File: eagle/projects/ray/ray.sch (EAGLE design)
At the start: 4 parts

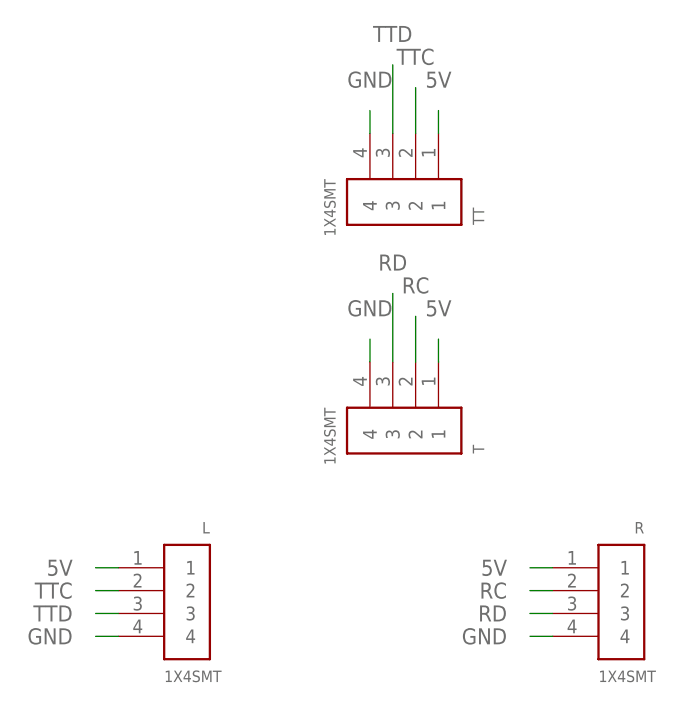
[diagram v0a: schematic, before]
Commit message: make solder pads for LED strips more forgiving
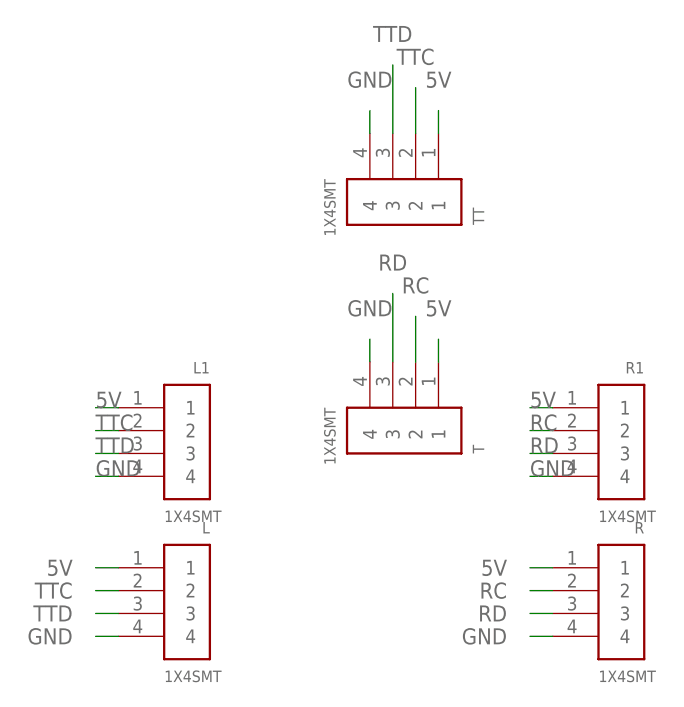
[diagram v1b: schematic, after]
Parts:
- added L1, R1: 1X4SMT, adafruit:1X4SMT
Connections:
- net 5V: now also L1.1, R1.1
- net GND: now also L1.4, R1.4
- net RC: now also R1.2
- net RD: now also R1.3
- net TTC: now also L1.2
- net TTD: now also L1.3
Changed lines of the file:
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@@
 <part name="R" library="adafruit" library_urn="urn:adsk.eagle:library:420" deviceset="1X4" device="SMT" package3d_urn="urn:adsk.eagle:package:6240933/1"/>
 <part name="TT" library="adafruit" library_urn="urn:adsk.eagle:library:420" deviceset="1X4" device="SMT" package3d_urn="urn:adsk.eagle:package:6240933/1"/>
+<part name="L1" library="adafruit" library_urn="urn:adsk.eagle:library:420" deviceset="1X4" device="SMT" package3d_urn="urn:adsk.eagle:package:6240933/1"/>
+<part name="R1" library="adafruit" library_urn="urn:adsk.eagle:library:420" deviceset="1X4" device="SMT" package3d_urn="urn:adsk.eagle:package:6240933/1"/>
 </parts>
 <sheets>
@@
 <attribute name="NAME" x="63.5" y="99.06" size="1.27" layer="95" font="vector" rot="R90"/>
 <attribute name="VALUE" x="45.72" y="104.14" size="1.27" layer="96" font="vector" rot="R270"/>
+</instance>
+<instance part="L1" gate="G$1" x="27.94" y="76.2" smashed="yes">
+<attribute name="NAME" x="33.02" y="83.82" size="1.27" layer="95" font="vector" rot="R180"/>
+<attribute name="VALUE" x="27.94" y="66.04" size="1.27" layer="96" font="vector"/>
+</instance>
+<instance part="R1" gate="G$1" x="76.2" y="76.2" smashed="yes">
+<attribute name="NAME" x="81.28" y="83.82" size="1.27" layer="95" font="vector" rot="R180"/>
+<attribute name="VALUE" x="76.2" y="66.04" size="1.27" layer="96" font="vector"/>
 </instance>
 </instances>
@@
 <label x="17.78" y="60.96" size="1.778" layer="95" align="center-right"/>
 </segment>
+<segment>
+<pinref part="L1" gate="G$1" pin="1"/>
+<wire x1="22.86" y1="78.74" x2="20.32" y2="78.74" width="0.1524" layer="91"/>
+<label x="20.32" y="78.74" size="1.778" layer="95"/>
+</segment>
+<segment>
+<pinref part="R1" gate="G$1" pin="1"/>
+<wire x1="71.12" y1="78.74" x2="68.58" y2="78.74" width="0.1524" layer="91"/>
+<label x="68.58" y="78.74" size="1.778" layer="95"/>
+</segment>
 </net>
 <net name="GND" class="0">
@@
 <label x="50.8" y="114.3" size="1.778" layer="95" align="bottom-center"/>
 </segment>
+<segment>
+<pinref part="L1" gate="G$1" pin="4"/>
+<wire x1="22.86" y1="71.12" x2="20.32" y2="71.12" width="0.1524" layer="91"/>
+<label x="20.32" y="71.12" size="1.778" layer="95"/>
+</segment>
+<segment>
+<pinref part="R1" gate="G$1" pin="4"/>
+<wire x1="71.12" y1="71.12" x2="68.58" y2="71.12" width="0.1524" layer="91"/>
+<label x="68.58" y="71.12" size="1.778" layer="95"/>
+</segment>
 </net>
 <net name="TTC" class="0">
@@
 <wire x1="22.86" y1="58.42" x2="20.32" y2="58.42" width="0.1524" layer="91"/>
 <label x="17.78" y="58.42" size="1.778" layer="95" align="center-right"/>
+</segment>
+<segment>
+<pinref part="L1" gate="G$1" pin="2"/>
+<wire x1="22.86" y1="76.2" x2="20.32" y2="76.2" width="0.1524" layer="91"/>
+<label x="20.32" y="76.2" size="1.778" layer="95"/>
 </segment>
 </net>
@@
 <label x="17.78" y="55.88" size="1.778" layer="95" align="center-right"/>
 </segment>
+<segment>
+<pinref part="L1" gate="G$1" pin="3"/>
+<wire x1="22.86" y1="73.66" x2="20.32" y2="73.66" width="0.1524" layer="91"/>
+<label x="20.32" y="73.66" size="1.778" layer="95"/>
+</segment>
 </net>
 <net name="RC" class="0">
@@
 <wire x1="55.88" y1="83.82" x2="55.88" y2="88.9" width="0.1524" layer="91"/>
 <label x="55.88" y="91.44" size="1.778" layer="95" align="bottom-center"/>
+</segment>
+<segment>
+<pinref part="R1" gate="G$1" pin="2"/>
+<wire x1="71.12" y1="76.2" x2="68.58" y2="76.2" width="0.1524" layer="91"/>
+<label x="68.58" y="76.2" size="1.778" layer="95"/>
 </segment>
 </net>
@@
 <label x="53.34" y="93.98" size="1.778" layer="95" align="bottom-center"/>
 </segment>
+<segment>
+<pinref part="R1" gate="G$1" pin="3"/>
+<wire x1="71.12" y1="73.66" x2="68.58" y2="73.66" width="0.1524" layer="91"/>
+<label x="68.58" y="73.66" size="1.778" layer="95"/>
+</segment>
 </net>
